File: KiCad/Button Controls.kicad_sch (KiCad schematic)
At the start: 8 parts, among them J3 691137710003, J4 691137710002, SW1 SW_Push, SW2 SW_Push, SW3 SW_Push

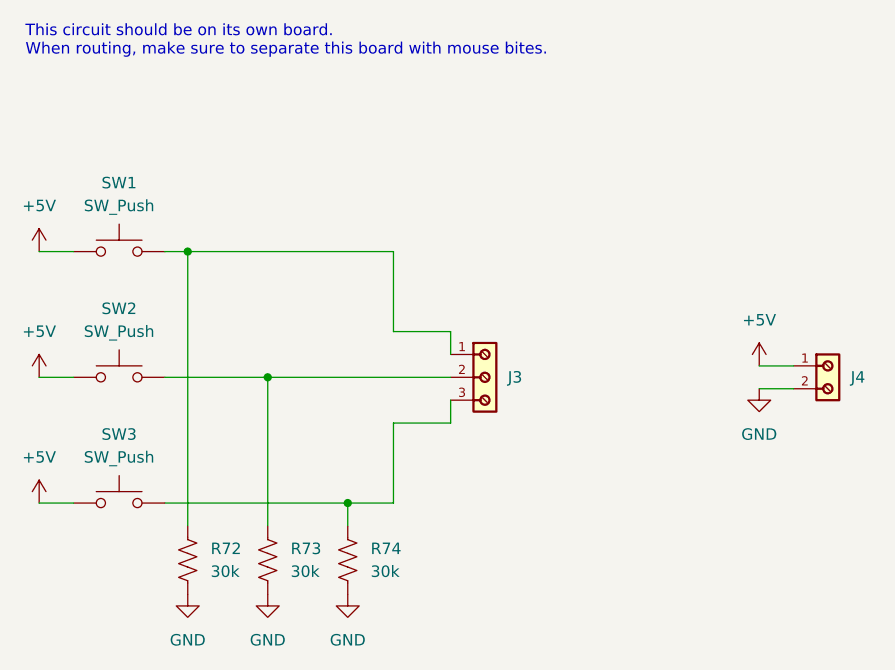
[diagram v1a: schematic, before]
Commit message: added power switch, decoupling caps, and unused IC pins
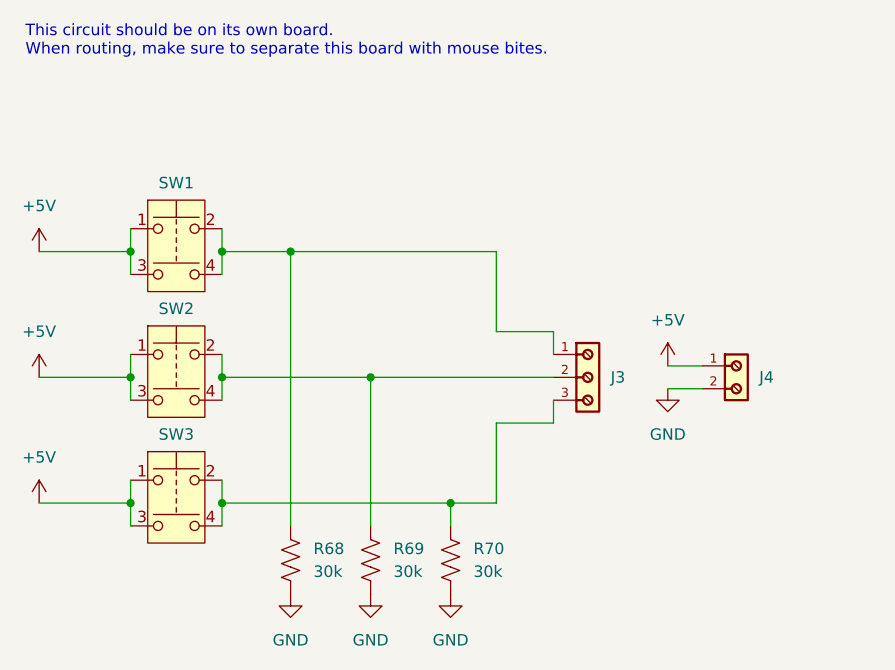
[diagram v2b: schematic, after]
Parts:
- removed SW1, SW2, SW3: SW_Push, Switch Push Button D6R90F2LFS:D6R90_CNK, symbol Switch:SW_Push
- added SW1, SW2, SW3: SW_Push_Dual, Switch Push Button D6R90F2LFS:D6R90_CNK, symbol Switch:SW_Push_Dual
- renumbered R72 to R68, R73 to R69, R74 to R70
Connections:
- net +5V: now also SW1.1, SW1.3, SW2.1, SW2.3, SW3.1, SW3.3
- net at J3.2, R69.1: now also SW2.2, SW2.4
- net at J3.1, R68.1: now also SW1.2, SW1.4
- net at J3.3, R70.1: now also SW3.2, SW3.4
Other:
- moved on the sheet: J3, J4, R68, R69, R70
